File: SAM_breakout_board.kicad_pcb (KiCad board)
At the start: 2 copper layers, 74.9 x 74.9 mm, 56 parts, among them J1 Conn_01x04, J10 Conn_01x12, J11 Conn_01x12, J2 Conn_01x04, J3 Conn_01x02, J4 USB_B_Micro, J5 Conn_ARM_JTAG_SWD_10, J6 Conn_01x04, J7 Conn_01x04, J8 Conn_01x02, J9 Conn_01x12, SW1 BATT_PWR, SW2 RST_SW, SW3 MAIN_PWR, U1 TPS62163DSG, U2 TPS63060, U3 ATSAMD21G18A-AUT, Y1 Crystal_ABS

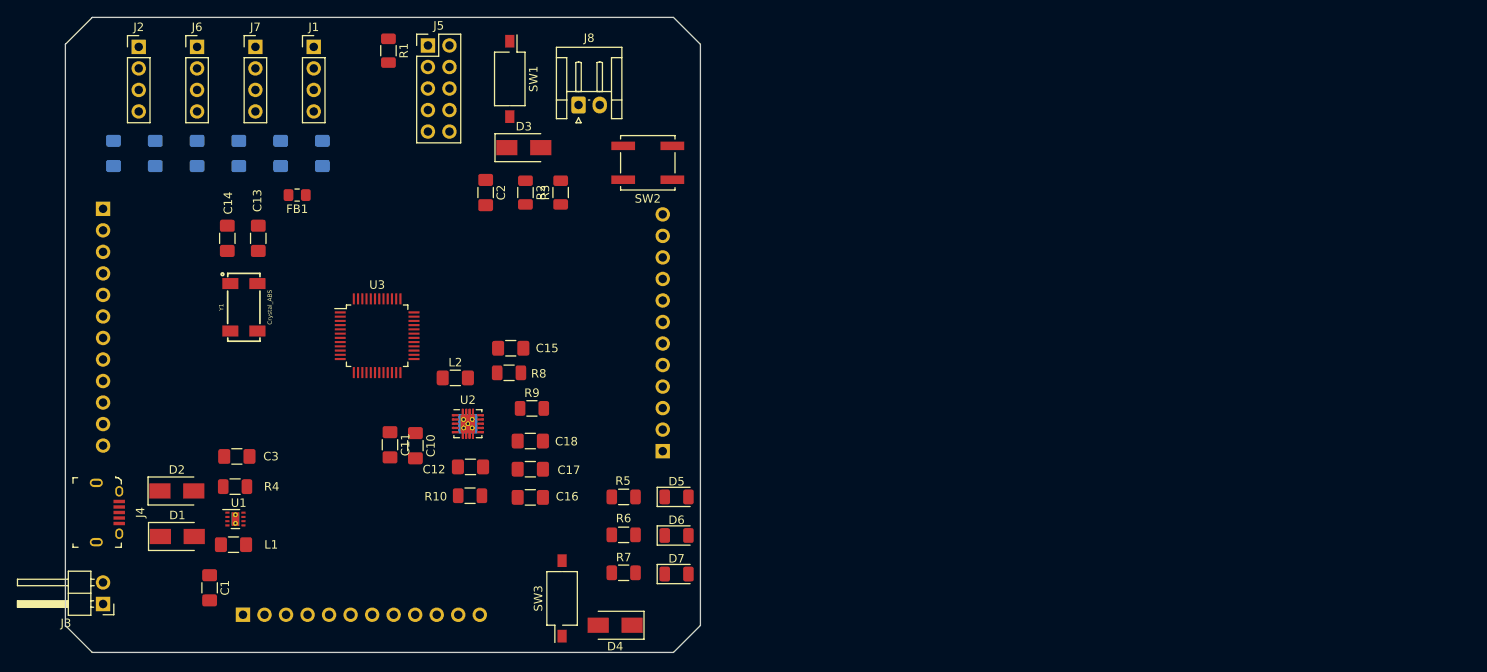
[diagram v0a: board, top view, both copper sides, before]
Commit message: Modification of footprints
Modified the footprints of the programmer header to be the correct pitch
Changed the JST connector to a generic 2 pin connector. The pitch of the
JST connector for it did not exist as a footprint, so chose one that fit
the online options. Further verification is needed for this.
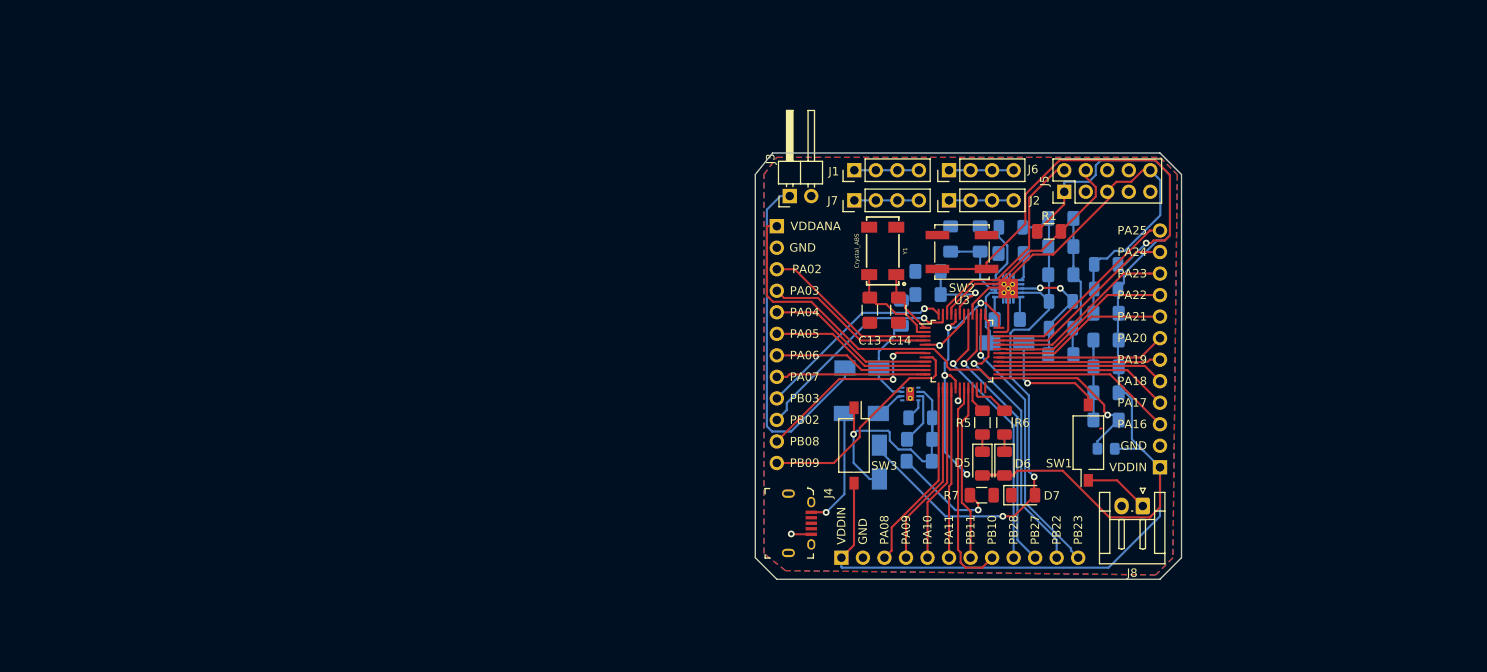
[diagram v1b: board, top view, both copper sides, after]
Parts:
- C1, C10, C11, C12, C15, C16, C17, C18, C2, C3, D1, D2, D3, D4, FB1, L1, L2, R10, R2, R3, R4, R8, R9, U1, U2: moved to B.Cu
- moved C7 109.5 mm to (162.8, 90.1), turned to 180 degrees
- moved C6 105.4 mm to (162.8, 93.3), turned to 180 degrees
- moved C5 102.3 mm to (162.8, 99.6), turned to 180 degrees
- moved FB1 100.0 mm to (162.8, 103.0), turned to 0 degrees
- moved J2 97.3 mm to (144.3, 73.7), turned to 90 degrees
- moved C9 97.1 mm to (141.8, 82.0), turned to 180 degrees
- moved C4 96.7 mm to (162.8, 96.4), turned to 180 degrees
- moved J3 94.2 mm to (125.5, 73.2), turned to 90 degrees
- moved C8 92.7 mm to (141.8, 84.8), turned to 180 degrees
- moved J6 89.9 mm to (144.3, 70.1), turned to 90 degrees
- moved C1 87.8 mm to (138.7, 87.0), turned to 90 degrees
- moved D1 83.2 mm to (134.0, 93.4)
- moved L1 81.9 mm to (140.8, 101.9)
- moved J8 81.7 mm to (167.1, 109.7), turned to 180 degrees
- moved J4 81.7 mm to (128.0, 111.8)
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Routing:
- net VDDIN: track 0.00 -> 185.8 mm, vias 0 -> 4
- net 5V_BATT: track 0.00 -> 67.3 mm, vias 0 -> 2
- net VDDANA: track 0.00 -> 62.1 mm, vias 0 -> 1
- net GND: track 0.00 -> 56.1 mm, vias 0 -> 4
- net Net-(R3-Pad2): track 0.00 -> 50.6 mm, vias 0 -> 1
- net RST: track 0.00 -> 50.3 mm
- net Net-(D1-Pad1): track 0.00 -> 42.2 mm
- net Net-(C3-Pad1): track 0.00 -> 34.7 mm, vias 0 -> 1
- net PB22: track 0.00 -> 34.2 mm, vias 0 -> 1
- net PB23: track 0.00 -> 33.5 mm, vias 0 -> 1
- net PA27: track 0.00 -> 32.8 mm, vias 0 -> 1
- net PA28: track 0.00 -> 32.4 mm, vias 0 -> 1
- net SWCLK: track 0.00 -> 26.8 mm
- net PB09: track 0.00 -> 26.8 mm
- net PB02: track 0.00 -> 26.2 mm, vias 0 -> 1
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- added copper zone on B.Cu, net GND
- added copper zone on F.Cu, net GND
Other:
- board size 74.9 x 74.9 mm -> 50.3 x 50.3 mm
- board text added: "GND"
- board text added: "PA02"
- board text added: "PA03"
- board text added: "PA04"
- board text added: "PA05"
- board text added: "PA06"
- board text added: "PA07"
- board text added: "PA08"
- board text added: "PA09"
- board text added: "PA10"
- board text added: "PA11"
- board text added: "PA16"
- board text added: "PA17"
- board text added: "PA18"
- board text added: "PA19"
- board text added: "PA20"
- board text added: "PA21"
- board text added: "PA22"
- board text added: "PA23"
- board text added: "PA24"
- board text added: "PA25"
- board text added: "PB02"
- board text added: "PB03"
- board text added: "PB08"
- board text added: "PB09"
- board text added: "PB10"
- board text added: "PB11"
- board text added: "PB22"
- board text added: "PB23"
- board text added: "PB27"
- board text added: "PB28"
- board text added: "VDDANA"
- board text added: "VDDIN"

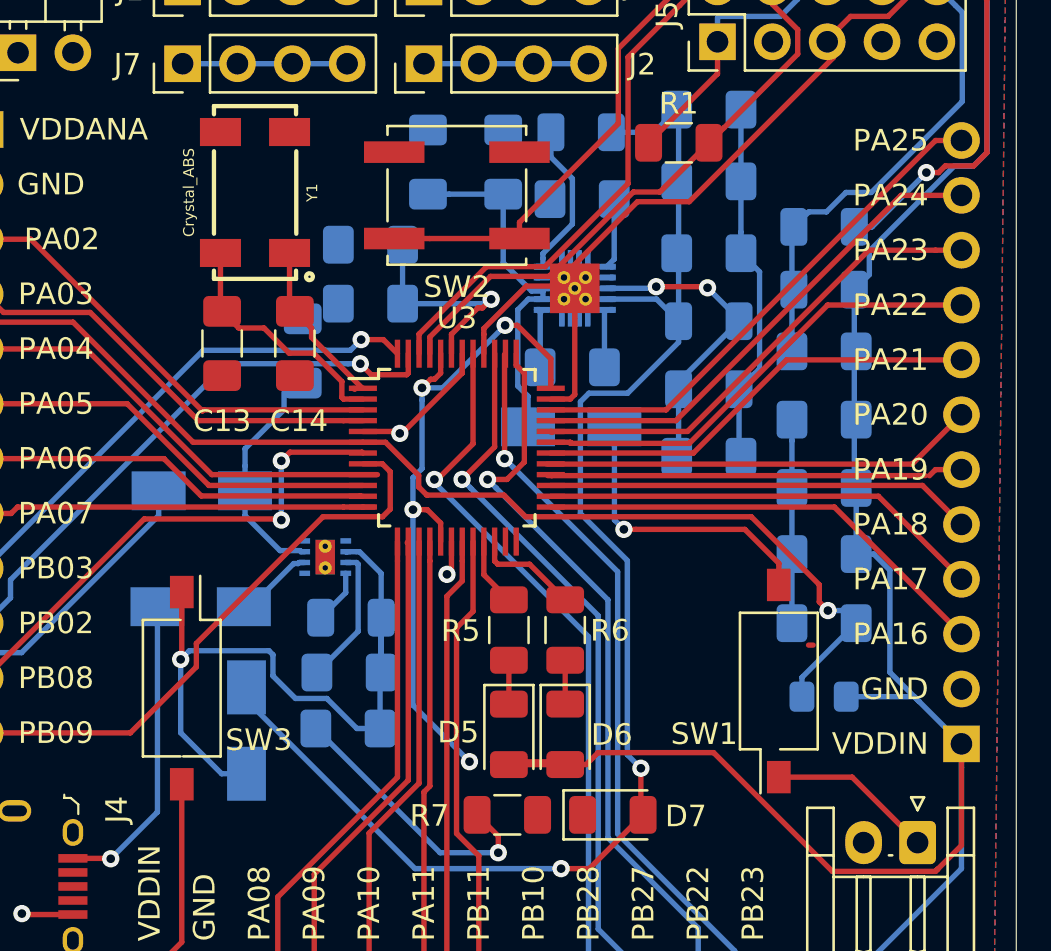
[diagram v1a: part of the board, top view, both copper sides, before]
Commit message: Changed Wiring
Changed the tracing in several different areas
moving conflicting components around to avoid conflicts of footprints

Need to:
remove aux rails
update footprints on power inputs
check circuitry to make sure routing is correct
check component U2 footprint and match with correct component
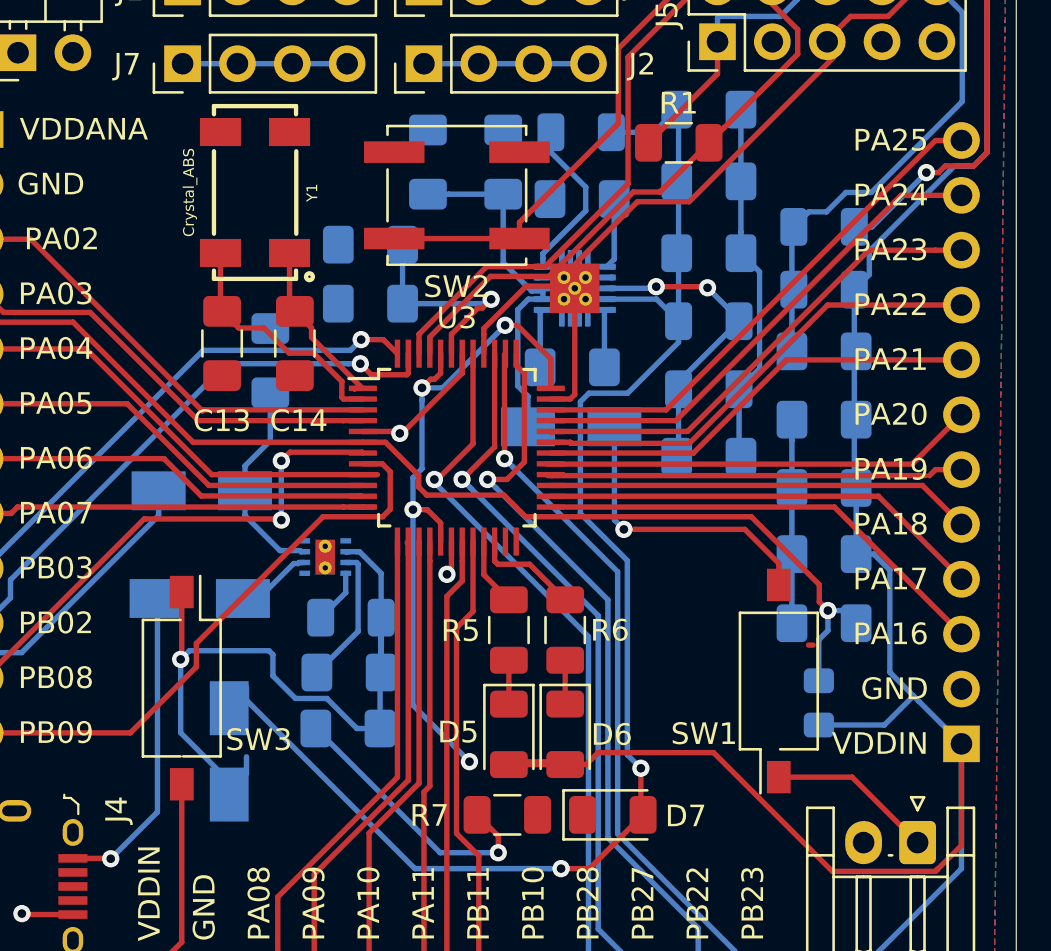
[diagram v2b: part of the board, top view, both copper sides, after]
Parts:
- moved C1 1.56 mm to (137.2, 87.4)
- moved D4 1.25 mm to (135.3, 105.5)
- moved D2 0.38 mm to (133.9, 98.4)
- moved FB1 0.38 mm to (162.6, 103.3), turned to 270 degrees
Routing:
- net VDDIN: track 185.8 -> 187.3 mm
- net VDDANA: track 62.1 -> 61.1 mm
- net Net-(R10-Pad1): track 7.20 -> 7.72 mm
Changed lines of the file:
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@@
-(kicad_pcb (version 20171130) (host pcbnew 5.1.4-3.fc30)
+(kicad_pcb (version 20171130) (host pcbnew "(5.1.4)-1")
   (general
     (thickness 1.6)
     (drawings 48)
-    (tracks 500)
+    (tracks 502)
     (zones 0)
     (modules 56)
@@
     (solder_mask_min_width 0.25)
     (aux_axis_origin 0 0)
-    (visible_elements FFFDFF7F)
+    (visible_elements 7FFFFFFF)
     (pcbplotparams
       (layerselection 0x010fc_ffffffff)
@@
   )
   (module Diode_SMD:D_SMA (layer B.Cu)
-    (at 136.0551 104.5403 270)
+    (at 135.255 105.505 270)
     (descr "Diode SMA (DO-214AC)")
     (tags "Diode SMA (DO-214AC)")
@@
   )
   (module Capacitor_SMD:C_1206_3216Metric_Pad1.42x1.75mm_HandSolder (layer B.Cu)
-    (at 138.6586 86.96198 90)
+    (at 137.16 87.4125 90)
     (descr "Capacitor SMD 1206 (3216 Metric), square (rectangular) end terminal, IPC_7351 nominal with elongated pad for handsoldering. (Body size source: http://www.tortai-tech.com/upload/download/2011102023233369053.pdf), generated with kicad-footprint-generator")
     (tags "capacitor handsolder")
@@
   )
   (module Diode_SMD:D_SMA (layer B.Cu)
-    (at 133.93064 98.806)
+    (at 133.89 98.425)
     (descr "Diode SMA (DO-214AC)")
     (tags "Diode SMA (DO-214AC)")
@@
   )
   (module Inductor_SMD:L_0805_2012Metric_Pad1.15x1.40mm_HandSolder (layer B.Cu)
-    (at 162.8013 102.9716)
+    (at 162.56 103.26 270)
     (descr "Capacitor SMD 0805 (2012 Metric), square (rectangular) end terminal, IPC_7351 nominal with elongated pad for handsoldering. (Body size source: https://docs.google.com/spreadsheets/d/1BsfQQcO9C6DZCsRaXUlFlo91Tg2WpOkGARC1WS5S8t0/edit?usp=sharing), generated with kicad-footprint-generator")
     (tags "inductor handsolder")
     (attr smd)
-    (fp_text reference FB1 (at 0 2.032 180) (layer B.SilkS)
+    (fp_text reference FB1 (at 0 2.032 270) (layer B.SilkS)
       (effects (font (size 1 1) (thickness 0.15)) (justify mirror))
     )
-    (fp_text value Ferrite_Bead_Small (at 0 -1.65) (layer B.Fab)
+    (fp_text value Ferrite_Bead_Small (at -0.7366 3.4163 90) (layer B.Fab)
       (effects (font (size 1 1) (thickness 0.15)) (justify mirror))
     )
@@
     (fp_line (start 1.85 0.95) (end 1.85 -0.95) (layer B.CrtYd) (width 0.05))
     (fp_line (start 1.85 -0.95) (end -1.85 -0.95) (layer B.CrtYd) (width 0.05))
-    (fp_text user %R (at 0 0) (layer B.Fab)
+    (fp_text user %R (at 0 0 90) (layer B.Fab)
       (effects (font (size 0.5 0.5) (thickness 0.08)) (justify mirror))
     )
-    (pad 1 smd roundrect (at -1.025 0) (size 1.15 1.4) (layers B.Cu B.Paste B.Mask) (roundrect_rratio 0.217391)
+    (pad 1 smd roundrect (at -1.025 0 270) (size 1.15 1.4) (layers B.Cu B.Paste B.Mask) (roundrect_rratio 0.217391)
       (net 6 VDDANA))
-    (pad 2 smd roundrect (at 1.025 0) (size 1.15 1.4) (layers B.Cu B.Paste B.Mask) (roundrect_rratio 0.217391)
+    (pad 2 smd roundrect (at 1.025 0 270) (size 1.15 1.4) (layers B.Cu B.Paste B.Mask) (roundrect_rratio 0.217391)
       (net 4 VDDIN))
     (model ${KISYS3DMOD}/Inductor_SMD.3dshapes/L_0805_2012Metric.wrl
@@
   (gr_line (start 121.5 118.288) (end 171.5 118.288) (layer Eco1.User) (width 0.15))
   (segment (start 135.93064 98.806) (end 136.28064 98.806) (width 0.25) (layer B.Cu) (net 1))
-  (segment (start 135.98652 91.48956) (end 135.98652 92.28644) (width 0.25) (layer B.Cu) (net 1))
-  (segment (start 137.795 89.68108) (end 135.98652 91.48956) (width 0.25) (layer B.Cu) (net 1))
-  (segment (start 135.98652 92.28644) (end 135.98652 93.43644) (width 0.25) (layer B.Cu) (net 1))
-  (segment (start 137.795 88.86858) (end 137.795 89.68108) (width 0.25) (layer B.Cu) (net 1))
   (segment (start 138.4975 96.7573) (end 138.75 96.7573) (width 0.25) (layer B.Cu) (net 1))
   (segment (start 138.447501 96.807299) (end 138.4975 96.7573) (width 0.25) (layer B.Cu) (net 1))
@@
   (segment (start 138.5864 96.2573) (end 138.536401 96.207301) (width 0.25) (layer B.Cu) (net 1))
   (segment (start 138.75 96.2573) (end 138.5864 96.2573) (width 0.25) (layer B.Cu) (net 1))
+  (segment (start 135.98652 92.28644) (end 137.16 91.11296) (width 0.25) (layer B.Cu) (net 1))
+  (segment (start 135.98652 93.43644) (end 135.98652 92.28644) (width 0.25) (layer B.Cu) (net 1))
+  (segment (start 137.16 91.11296) (end 137.16 90.17) (width 0.25) (layer B.Cu) (net 1))
+  (segment (start 137.16 90.17) (end 137.16 88.9) (width 0.25) (layer B.Cu) (net 1))
   (via (at 145.3388 97.3074) (size 0.8) (drill 0.4) (layers F.Cu B.Cu) (net 2))
   (segment (start 151.256 85.4613) (end 151.256 84.0613) (width 0.25) (layer F.Cu) (net 2))
@@
   (via (at 144.1831 88.6714) (size 0.8) (drill 0.4) (layers F.Cu B.Cu) (net 4))
   (via (at 143.764 94.3102) (size 0.8) (drill 0.4) (layers F.Cu B.Cu) (net 4))
-  (segment (start 163.8263 102.9716) (end 166.9796 102.9716) (width 0.25) (layer B.Cu) (net 4))
   (segment (start 165.1013 96.3676) (end 165.8493 97.1156) (width 0.25) (layer B.Cu) (net 4))
   (segment (start 164.2888 96.3676) (end 165.1013 96.3676) (width 0.25) (layer B.Cu) (net 4))
-  (segment (start 165.8493 101.8413) (end 167.20185 103.19385) (width 0.25) (layer B.Cu) (net 4))
   (segment (start 165.8493 97.1156) (end 165.8493 101.8413) (width 0.25) (layer B.Cu) (net 4))
-  (segment (start 166.9796 102.9716) (end 167.20185 103.19385) (width 0.25) (layer B.Cu) (net 4))
   (segment (start 167.20185 103.19385) (end 169.164 105.156) (width 0.25) (layer B.Cu) (net 4))
   (segment (start 164.2888 93.3069) (end 164.2888 96.3676) (width 0.25) (layer B.Cu) (net 4))
@@
   (segment (start 143.764 103.3653) (end 146.3802 105.9815) (width 0.25) (layer B.Cu) (net 4))
   (segment (start 143.764 94.3102) (end 143.764 103.3653) (width 0.25) (layer B.Cu) (net 4))
+  (segment (start 165.59 104.285) (end 166.9415 102.9335) (width 0.25) (layer B.Cu) (net 4))
+  (segment (start 162.56 104.285) (end 165.59 104.285) (width 0.25) (layer B.Cu) (net 4))
+  (segment (start 165.8493 101.8413) (end 166.9415 102.9335) (width 0.25) (layer B.Cu) (net 4))
+  (segment (start 166.9415 102.9335) (end 167.20185 103.19385) (width 0.25) (layer B.Cu) (net 4))
   (via (at 133.0071 101.2444) (size 0.8) (drill 0.4) (layers F.Cu B.Cu) (net 5))
   (segment (start 142.24 101.9048) (end 142.2908 101.854) (width 0.25) (layer B.Cu) (net 5))
@@
   (segment (start 142.24 104.4448) (end 141.16569 104.4448) (width 0.25) (layer B.Cu) (net 5))
   (via (at 162.9791 98.9838) (size 0.8) (drill 0.4) (layers F.Cu B.Cu) (net 6))
-  (segment (start 161.7763 102.0805) (end 161.7763 102.9716) (width 0.25) (layer B.Cu) (net 6))
-  (segment (start 164.2888 99.568) (end 161.7763 102.0805) (width 0.25) (layer B.Cu) (net 6))
   (segment (start 163.7046 98.9838) (end 164.2888 99.568) (width 0.25) (layer B.Cu) (net 6))
   (segment (start 162.9791 98.9838) (end 163.7046 98.9838) (width 0.25) (layer B.Cu) (net 6))
@@
   (segment (start 144.029599 93.261201) (end 144.029599 92.727801) (width 0.25) (layer F.Cu) (net 6))
   (segment (start 159.433103 94.640001) (end 148.981099 94.640001) (width 0.25) (layer F.Cu) (net 6))
+  (segment (start 162.9791 98.9838) (end 162.9791 99.9109) (width 0.25) (layer B.Cu) (net 6))
+  (segment (start 162.56 100.33) (end 162.56 102.235) (width 0.25) (layer B.Cu) (net 6))
+  (segment (start 162.9791 99.9109) (end 162.56 100.33) (width 0.25) (layer B.Cu) (net 6))
   (via (at 147.3835 84.5693) (size 0.8) (drill 0.4) (layers F.Cu B.Cu) (net 7))
   (segment (start 143.283 82.04158) (end 143.283 84.7725) (width 0.25) (layer B.Cu) (net 7))
@@
   (segment (start 149.1645 96.8375) (end 147.6935 96.8375) (width 0.25) (layer F.Cu) (net 69))
   (segment (start 150.8125 98.4855) (end 149.1645 96.8375) (width 0.25) (layer F.Cu) (net 69))
-  (segment (start 149.782 82.6713) (end 149.782 83.0613) (width 0.25) (layer B.Cu) (net 70))
+  (segment (start 150.1521 77.7621) (end 151.765 79.375) (width 0.25) (layer B.Cu) (net 70))
+  (segment (start 150.1521 76.835) (end 150.1521 77.7621) (width 0.25) (layer B.Cu) (net 70))
+  (segment (start 151.765 79.375) (end 151.765 80.468298) (width 0.25) (layer B.Cu) (net 70))
+  (segment (start 151.765 80.468298) (end 149.782 82.451298) (width 0.25) (layer B.Cu) (net 70))
   (segment (start 149.782 82.451298) (end 149.782 82.6713) (width 0.25) (layer B.Cu) (net 70))
-  (segment (start 151.14563 78.98018) (end 151.14563 81.087668) (width 0.25) (layer B.Cu) (net 70))
-  (segment (start 151.14563 81.087668) (end 149.782 82.451298) (width 0.25) (layer B.Cu) (net 70))
-  (segment (start 150.1521 77.98665) (end 151.14563 78.98018) (width 0.25) (layer B.Cu) (net 70))
-  (segment (start 150.1521 76.835) (end 150.1521 77.98665) (width 0.25) (layer B.Cu) (net 70))
+  (segment (start 149.782 82.6713) (end 149.782 83.0613) (width 0.25) (layer B.Cu) (net 70))
   (zone (net 2) (net_name GND) (layer B.Cu) (hatch edge 0.508)
     (connect_pads (clearance 0.508))
